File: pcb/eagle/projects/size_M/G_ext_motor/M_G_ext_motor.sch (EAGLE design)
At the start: 11 parts

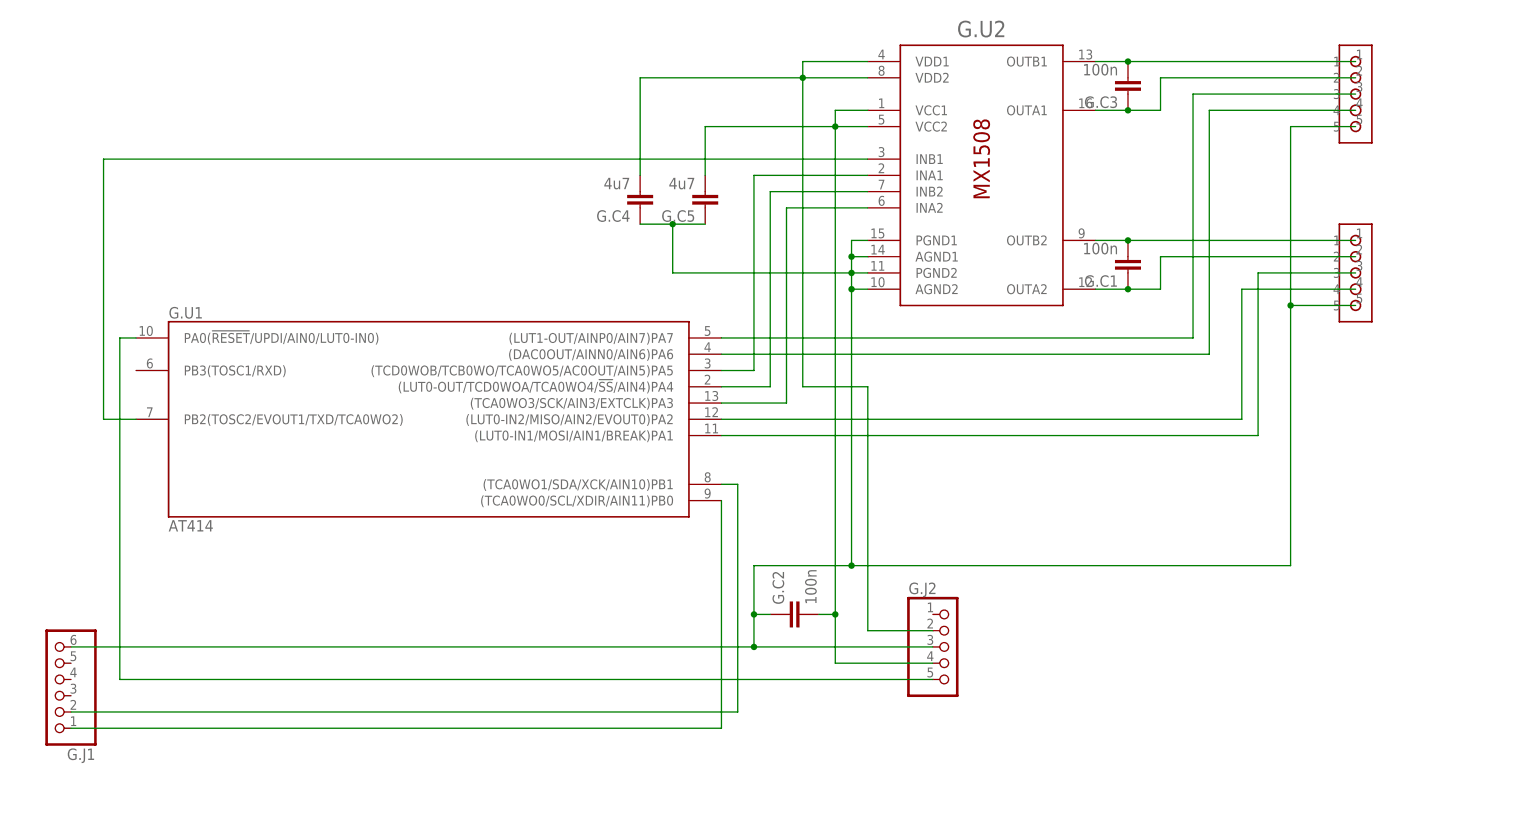
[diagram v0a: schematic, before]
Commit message: motor - path name adjustments
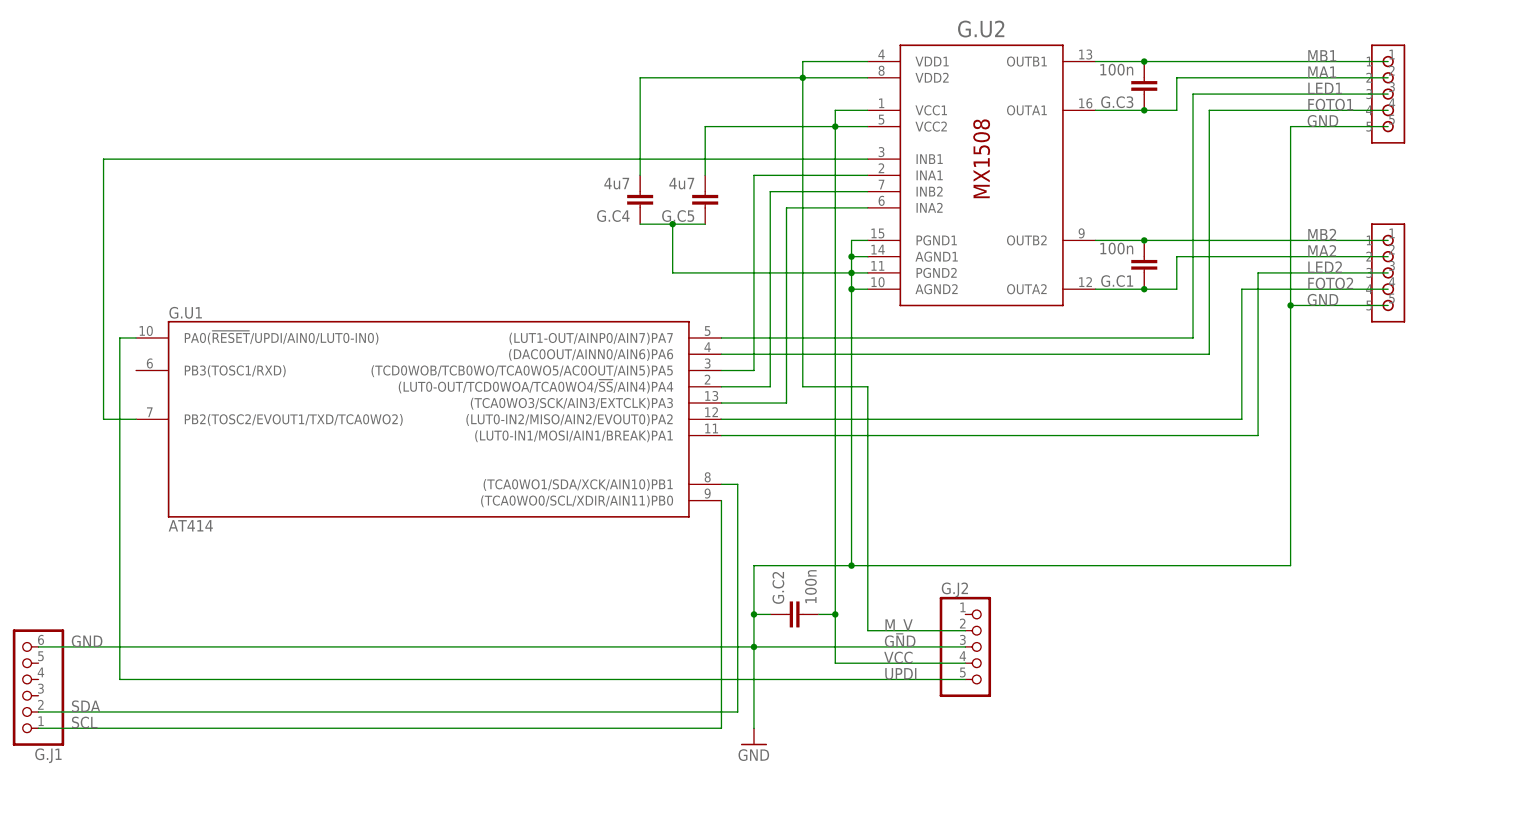
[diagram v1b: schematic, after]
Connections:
- net M1 renamed MB1
- net M2 renamed MA1
- net M3 renamed MB2
- net M4 renamed MA2
- net M_SRC renamed M_V
- net N$19 renamed SCL
- net N$20 renamed SDA
- net N$7 renamed UPDI
- net FOTO1: now also G.MOTO1.4, G.U1G$1.(DAC0OUT/AINN0/AIN6)PA6; no longer G.MOTO1.3, G.U1G$1.(LUT1-OUT/AINP0/AIN7)PA7
- net LED1: now also G.MOTO1.3, G.U1G$1.(LUT1-OUT/AINP0/AIN7)PA7; no longer G.MOTO1.4, G.U1G$1.(DAC0OUT/AINN0/AIN6)PA6
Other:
- moved on the sheet: G.C1, G.C3, G.J1, G.J2

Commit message: PCB M.1
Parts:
- G.J3, G.MOTO1: value A1250WR -> A1250WR-6; device hugo:A1250WR -> hugo:A1250WR-6
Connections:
- removed net FOTO1: G.MOTO1.4, G.U1G$1.(DAC0OUT/AINN0/AIN6)PA6
- removed net FOTO2: G.J3.4, G.U1G$1.(LUT0-IN2/MISO/AIN2/EVOUT0)PA2
- removed net LED1: G.MOTO1.3, G.U1G$1.(LUT1-OUT/AINP0/AIN7)PA7
- removed net LED2: G.J3.3, G.U1G$1.(LUT0-IN1/MOSI/AIN1/BREAK)PA1
- new net FOTOA1: G.MOTO1.5, G.U1G$1.(DAC0OUT/AINN0/AIN6)PA6
- new net FOTOA2: G.J3.5, G.U1G$1.(LUT0-IN2/MISO/AIN2/EVOUT0)PA2
- new net FOTOB1: G.MOTO1.4, G.U1G$1.(LUT1-OUT/AINP0/AIN7)PA7
- new net FOTOB2: G.J3.4, G.U1G$1.(LUT0-IN1/MOSI/AIN1/BREAK)PA1
- new net POWER: G.J3.3, G.MOTO1.3, G.U1G$1.PB3(TOSC1/RXD)
- net GND: now also G.J3.6, G.MOTO1.6; no longer G.J3.5, G.MOTO1.5
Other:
- moved on the sheet: G.C2, G.J1, G.J2, G.U1

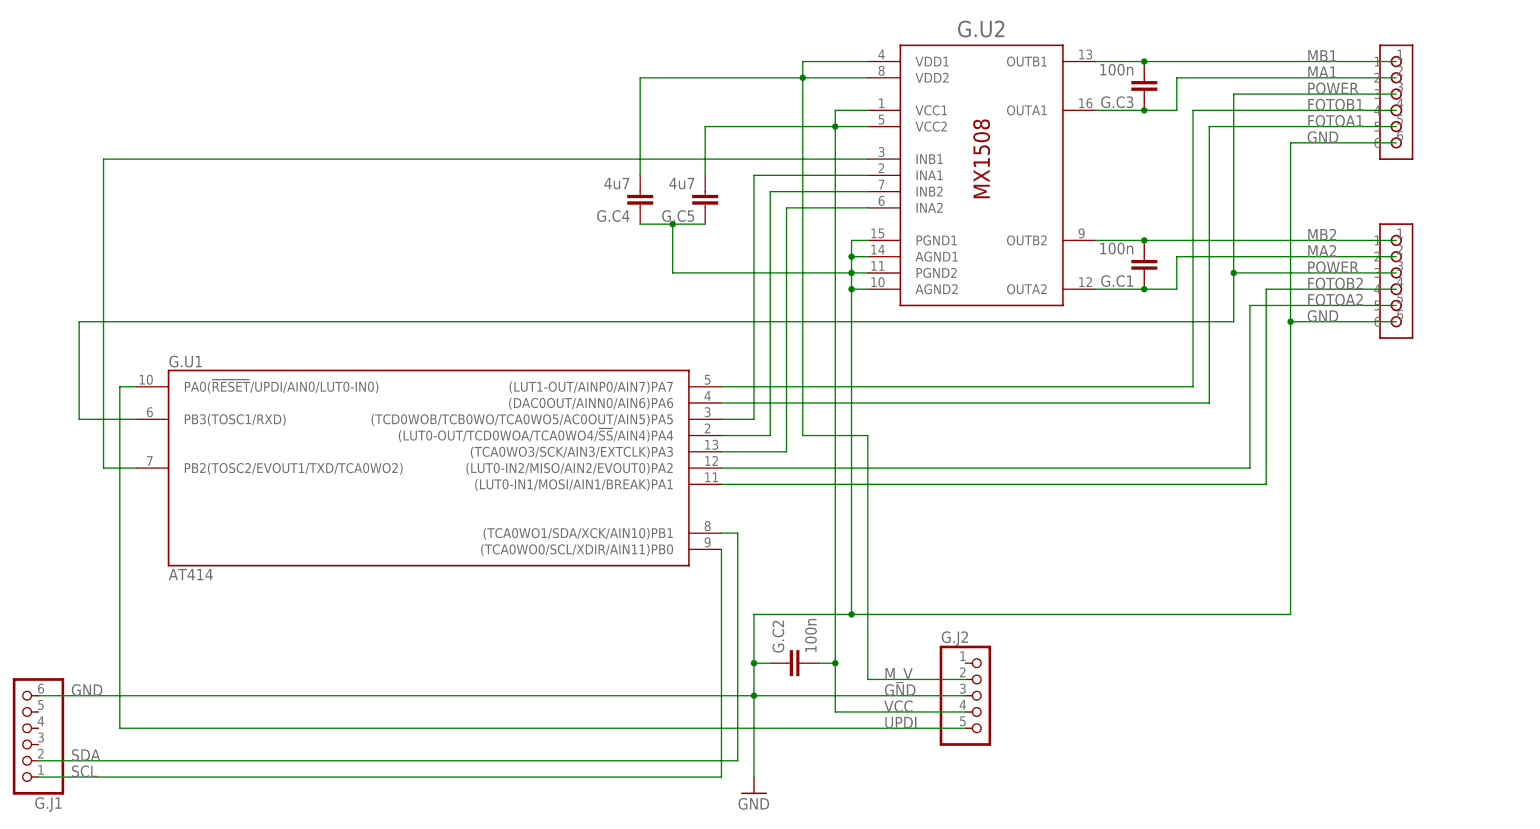
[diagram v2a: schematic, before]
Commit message: updated PCBs after delivery of v1
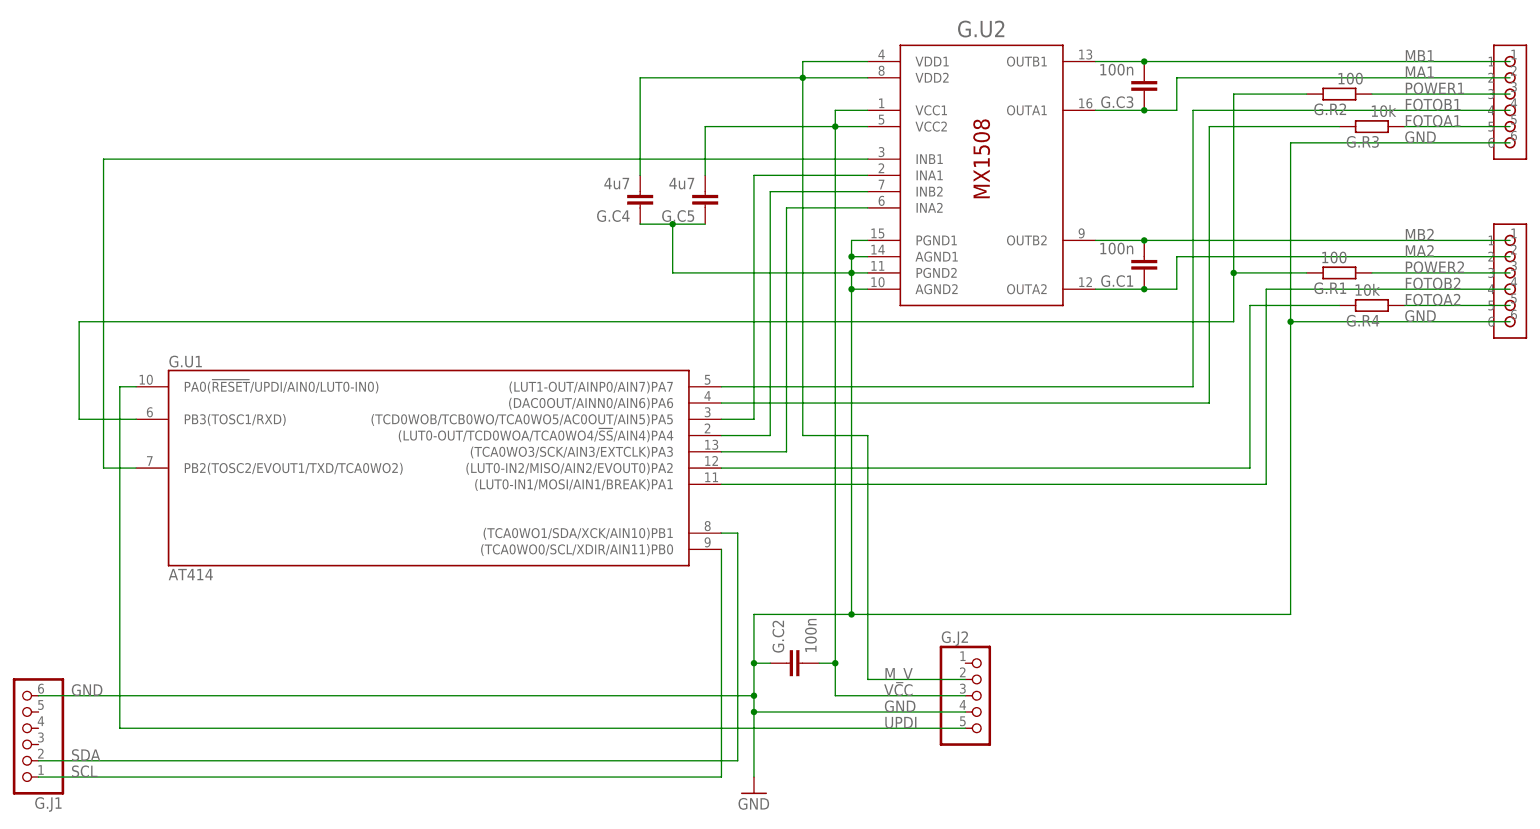
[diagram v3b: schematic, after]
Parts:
- added G.R1, G.R2: 100, rcl:R-EU_R0603
- added G.R3, G.R4: 10k, rcl:R-EU_R0603
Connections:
- removed net POWER: G.J3.3, G.MOTO1.3, G.U1G$1.PB3(TOSC1/RXD)
- new net POWER1: G.MOTO1.3, G.R2.1
- new net POWER2: G.J3.3, G.R1.1
- new net POWER_LED: G.R1.2, G.R2.2, G.U1G$1.PB3(TOSC1/RXD)
- new net _FOTOA1_: G.R3.2, G.U1G$1.(DAC0OUT/AINN0/AIN6)PA6
- new net _FOTOA2_: G.R4.2, G.U1G$1.(LUT0-IN2/MISO/AIN2/EVOUT0)PA2
- net FOTOA1: now also G.R3.1; no longer G.U1G$1.(DAC0OUT/AINN0/AIN6)PA6
- net FOTOA2: now also G.R4.1; no longer G.U1G$1.(LUT0-IN2/MISO/AIN2/EVOUT0)PA2
- net GND: now also G.J2.4; no longer G.J2.3
- net VCC: now also G.J2.3; no longer G.J2.4

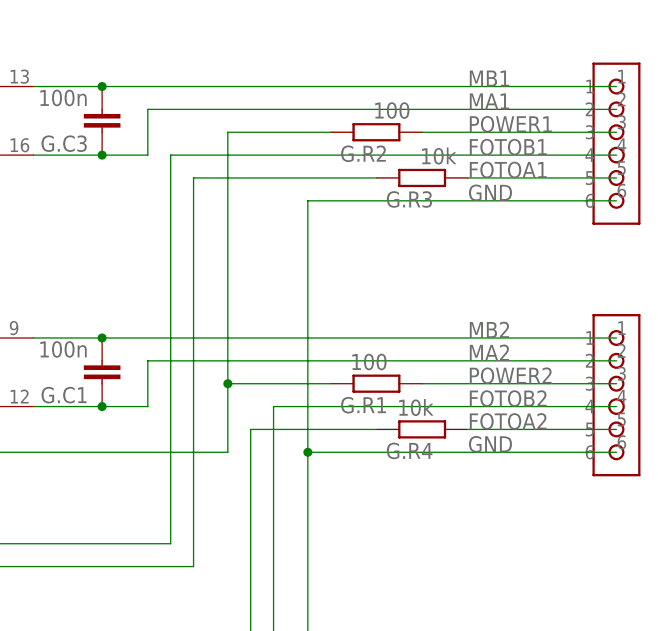
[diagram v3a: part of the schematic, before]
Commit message: button block + chassis + default i2c addresses
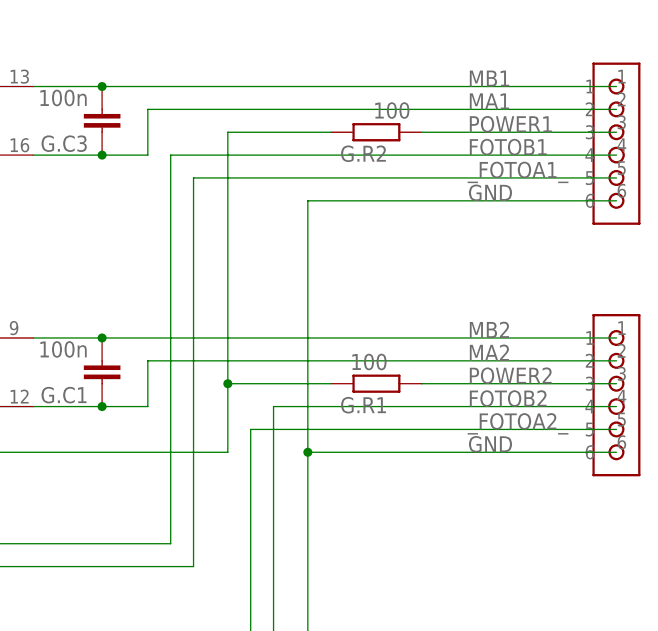
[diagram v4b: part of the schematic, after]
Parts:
- removed G.R3, G.R4: 10k, rcl:R-EU_R0603
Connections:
- removed net FOTOA1: G.MOTO1.5, G.R3.1
- removed net FOTOA2: G.J3.5, G.R4.1
- net _FOTOA1_: now also G.MOTO1.5; no longer G.R3.2
- net _FOTOA2_: now also G.J3.5; no longer G.R4.2
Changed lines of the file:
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@@
 <part name="G.R1" library="rcl" library_urn="urn:adsk.eagle:library:334" deviceset="R-EU_" device="R0603" package3d_urn="urn:adsk.eagle:package:23555/3" value="100"/>
 <part name="G.R2" library="rcl" library_urn="urn:adsk.eagle:library:334" deviceset="R-EU_" device="R0603" package3d_urn="urn:adsk.eagle:package:23555/3" value="100"/>
-<part name="G.R3" library="rcl" library_urn="urn:adsk.eagle:library:334" deviceset="R-EU_" device="R0603" package3d_urn="urn:adsk.eagle:package:23555/3" value="10k"/>
-<part name="G.R4" library="rcl" library_urn="urn:adsk.eagle:library:334" deviceset="R-EU_" device="R0603" package3d_urn="urn:adsk.eagle:package:23555/3" value="10k"/>
 </parts>
 <sheets>
@@
 <attribute name="NAME" x="130.81" y="155.9814" size="1.778" layer="95" rot="R180"/>
 <attribute name="VALUE" x="133.35" y="160.782" size="1.778" layer="96" rot="R180"/>
-</instance>
-<instance part="G.R3" gate="G$1" x="134.62" y="152.4" smashed="yes" rot="R180">
-<attribute name="NAME" x="135.89" y="150.9014" size="1.778" layer="95" rot="R180"/>
-<attribute name="VALUE" x="138.43" y="155.702" size="1.778" layer="96" rot="R180"/>
-</instance>
-<instance part="G.R4" gate="G$1" x="134.62" y="124.46" smashed="yes" rot="R180">
-<attribute name="NAME" x="135.89" y="122.9614" size="1.778" layer="95" rot="R180"/>
-<attribute name="VALUE" x="135.89" y="127.762" size="1.778" layer="96" rot="R180"/>
 </instance>
 </instances>
@@
 <wire x1="33.02" y1="99.06" x2="115.57" y2="99.06" width="0.1524" layer="91"/>
 <wire x1="115.57" y1="99.06" x2="115.57" y2="124.46" width="0.1524" layer="91"/>
-<wire x1="115.57" y1="124.46" x2="129.54" y2="124.46" width="0.1524" layer="91"/>
-<pinref part="G.R4" gate="G$1" pin="2"/>
+<wire x1="115.57" y1="124.46" x2="156.21" y2="124.46" width="0.1524" layer="91"/>
+<pinref part="G.J3" gate="G$1" pin="5"/>
+<label x="139.7" y="124.46" size="1.778" layer="95"/>
 </segment>
 </net>
@@
 <wire x1="109.22" y1="109.22" x2="33.02" y2="109.22" width="0.1524" layer="91"/>
 <wire x1="109.22" y1="152.4" x2="109.22" y2="109.22" width="0.1524" layer="91"/>
-<wire x1="129.54" y1="152.4" x2="109.22" y2="152.4" width="0.1524" layer="91"/>
-<pinref part="G.R3" gate="G$1" pin="2"/>
+<wire x1="156.21" y1="152.4" x2="109.22" y2="152.4" width="0.1524" layer="91"/>
+<pinref part="G.MOTO1" gate="G$1" pin="5"/>
+<label x="139.7" y="152.4" size="1.778" layer="95"/>
 </segment>
 </net>
@@
 </segment>
 </net>
-<net name="FOTOA1" class="0">
-<segment>
-<pinref part="G.MOTO1" gate="G$1" pin="5"/>
-<wire x1="156.21" y1="152.4" x2="139.7" y2="152.4" width="0.1524" layer="91"/>
-<pinref part="G.R3" gate="G$1" pin="1"/>
-<label x="139.7" y="152.4" size="1.778" layer="95"/>
-</segment>
-</net>
 <net name="POWER1" class="0">
 <segment>
@@
 </segment>
 </net>
-<net name="FOTOA2" class="0">
-<segment>
-<pinref part="G.J3" gate="G$1" pin="5"/>
-<wire x1="139.7" y1="124.46" x2="156.21" y2="124.46" width="0.1524" layer="91"/>
-<pinref part="G.R4" gate="G$1" pin="1"/>
-<label x="139.7" y="124.46" size="1.778" layer="95"/>
-</segment>
-</net>

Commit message: PCB v7 * 14 pin attiny is main adapter chip now. * changed adapter pin meaning (a1-a5, swapped RX-TX, VUSB replaced by A5, top most pin changed from GND to A4) * changed usb chip of main board
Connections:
- net GND: no longer G.J1.6
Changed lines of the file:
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@@
 <wire x1="53.34" y1="127" x2="53.34" y2="129.54" width="0.1524" layer="91"/>
 <junction x="53.34" y="127"/>
-<pinref part="G.J1" gate="A" pin="6"/>
-<wire x1="-73.66" y1="63.5" x2="38.1" y2="63.5" width="0.1524" layer="91"/>
-<wire x1="38.1" y1="63.5" x2="38.1" y2="68.58" width="0.1524" layer="91"/>
+<wire x1="38.1" y1="60.96" x2="38.1" y2="68.58" width="0.1524" layer="91"/>
 <junction x="38.1" y="68.58"/>
-<junction x="38.1" y="63.5"/>
 <pinref part="G.C4" gate="G$1" pin="1"/>
 <pinref part="G.C5" gate="G$1" pin="1"/>
@@
 <wire x1="38.1" y1="50.8" x2="38.1" y2="60.96" width="0.1524" layer="91"/>
 <label x="58.42" y="60.96" size="1.778" layer="95"/>
-<label x="-68.58" y="63.5" size="1.778" layer="95"/>
 <label x="139.7" y="149.86" size="1.778" layer="95"/>
 <label x="139.7" y="121.92" size="1.778" layer="95"/>
 <pinref part="G.J3" gate="G$1" pin="6"/>
-<wire x1="38.1" y1="60.96" x2="38.1" y2="63.5" width="0.1524" layer="91"/>
 <wire x1="156.21" y1="121.92" x2="121.92" y2="121.92" width="0.1524" layer="91"/>
 <junction x="121.92" y="121.92"/>
